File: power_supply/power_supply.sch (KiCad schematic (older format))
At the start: 39 parts, among them J1 Conn_01x04_Male, J2 Conn_01x03_Male, J3 Conn_01x03_Male, J4 Conn_01x03_Male, U1 LM7815_TO220, U2 LM7915_TO220, U3 LM7805_TO220

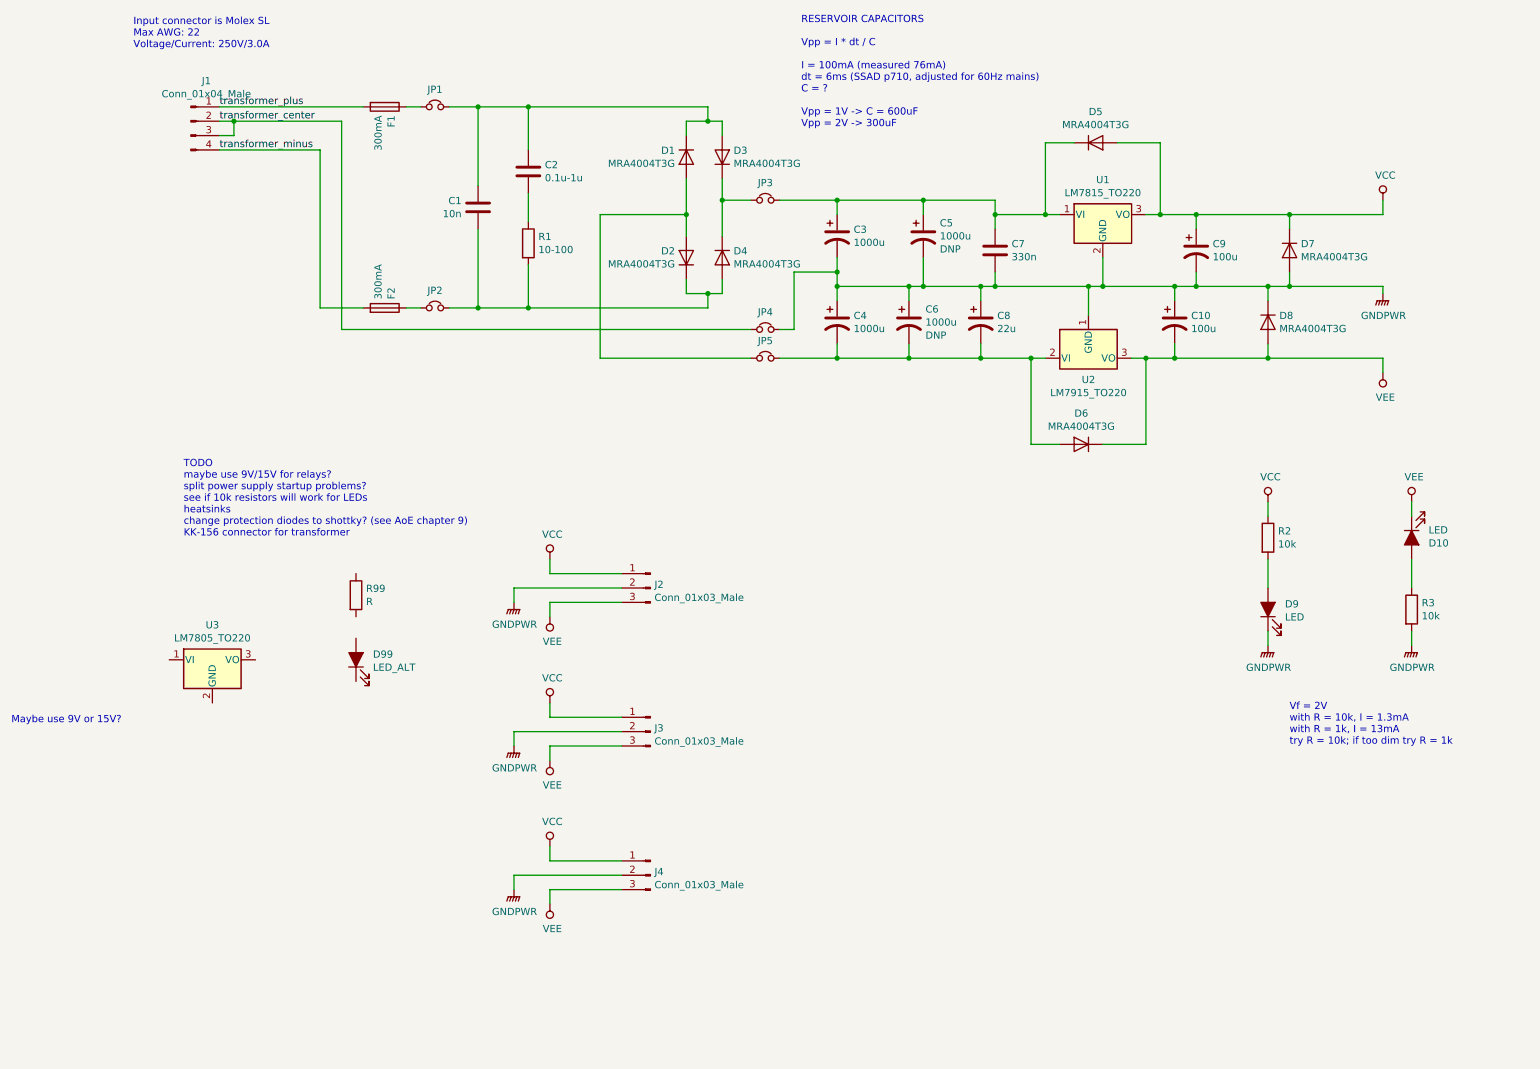
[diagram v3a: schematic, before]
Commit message: Update power supply layout & schematic
- Update snubber capacitor circuit details
- add heatsinks & mounting holes to schematic (footprints incorrect or
missing)
- initial component placement in layout
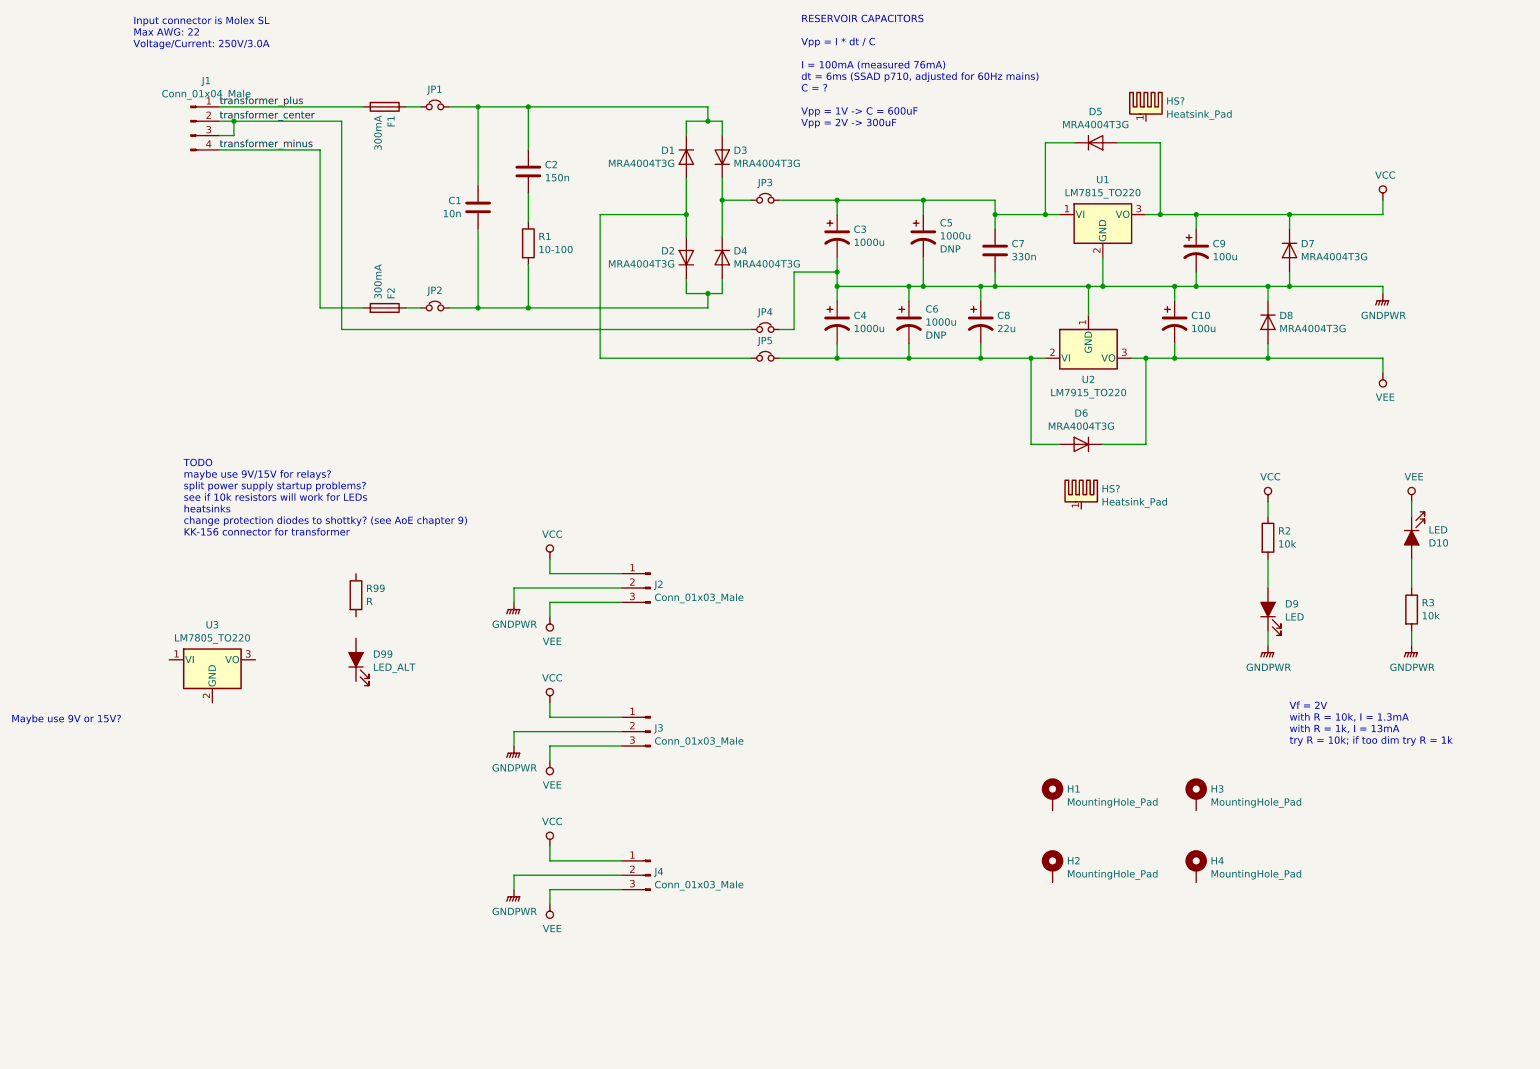
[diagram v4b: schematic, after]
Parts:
- added H1, H2, H3, H4: MountingHole_Pad, MountingHole:MountingHole_4.3mm_M4_Pad, symbol Mechanical:MountingHole_Pad
- added HS? (x2): Heatsink_Pad, symbol Mechanical:Heatsink_Pad
- C1: footprint (none) -> Capacitor_THT:C_Rect_L7.2mm_W2.5mm_P5.00mm_FKS2_FKP2_MKS2_MKP2; Distributor (none) -> Digikey; Distributor PN (none) -> 495-1180-ND; Manufacturer (none) -> EPCOS; Manufacturer PN (none) -> B32529C3103J000; URL (none) -> https://www.digikey.com/product-detail/en/B32529C3103J000/4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; Unit Price (none) -> 0.31
- C2: value 0.1u-1u -> 150n; footprint (none) -> Capacitor_THT:C_Rect_L7.5mm_W6.5mm_P5.00mm; Distributor (none) -> Digikey; Distributor PN (none) -> 495-2535-ND; Manufacturer (none) -> EPCOS; Manufacturer PN (none) -> B32529C3154K000; URL (none) -> https://www.digikey.com/product-detail/en/B32529C3154K000/4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; Unit Price (none) -> 0.63
- R1: footprint (none) -> Resistor_SMD:R_1206_3216Metric_Pad1.42x1.75mm_HandSolder
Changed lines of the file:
@@
 P 3350 1700
 F 0 "C2" H 3465 1746 50  0000 L CNN
-F 1 "0.1u-1u" H 3465 1655 50  0000 L CNN
-F 2 "" H 3388 1550 50  0001 C CNN
-F 3 "~" H 3350 1700 50  0001 C CNN
+F 1 "150n" H 3465 1655 50  0000 L CNN
+F 2 "Capacitor_THT:C_Rect_L7.5mm_W6.5mm_P5.00mm" H 3388 1550 50  0001 C CNN
+F 3 "https://www.tdk-electronics.tdk.com/inf/20/20/db/fc_2009/B32520_529.pdf" H 3350 1700 50  0001 C CNN
+F 4 "EPCOS" H 3350 1700 50  0001 C CNN "Manufacturer"
+F 5 "B32529C3154K000" H 3350 1700 50  0001 C CNN "Manufacturer PN"
+F 6 "Digikey" H 3350 1700 50  0001 C CNN "Distributor"
+F 7 "495-2535-ND" H 3350 1700 50  0001 C CNN "Distributor PN"
+F 8 "https://www.digikey.com/product-detail/en/B32529C3154K000/495-2535-ND/1089815/?itemSeq=288794403" H 3350 1700 50  0001 C CNN "URL"
+F 9 "0.63" H 3350 1700 50  0001 C CNN "Unit Price"
 	1    3350 1700
 	1    0    0    -1
@@
 F 0 "R1" H 3420 2246 50  0000 L CNN
 F 1 "10-100" H 3420 2155 50  0000 L CNN
-F 2 "" V 3280 2200 50  0001 C CNN
+F 2 "Resistor_SMD:R_1206_3216Metric_Pad1.42x1.75mm_HandSolder" V 3280 2200 50  0001 C CNN
 F 3 "~" H 3350 2200 50  0001 C CNN
 	1    3350 2200
@@
 F 0 "C1" H 3115 1996 50  0000 L CNN
 F 1 "10n" H 3115 1905 50  0000 L CNN
-F 2 "" H 3038 1800 50  0001 C CNN
-F 3 "~" H 3000 1950 50  0001 C CNN
+F 2 "Capacitor_THT:C_Rect_L7.2mm_W2.5mm_P5.00mm_FKS2_FKP2_MKS2_MKP2" H 3038 1800 50  0001 C CNN
+F 3 "https://www.tdk-electronics.tdk.com/inf/20/20/db/fc_2009/B32520_529.pdf" H 3000 1950 50  0001 C CNN
+F 4 "EPCOS" H 3000 1950 50  0001 C CNN "Manufacturer"
+F 5 "B32529C3103J000" H 3000 1950 50  0001 C CNN "Manufacturer PN"
+F 6 "Digikey" H 3000 1950 50  0001 C CNN "Distributor"
+F 7 "495-1180-ND" H 3000 1950 50  0001 C CNN "Distributor PN"
+F 8 "https://www.digikey.com/product-detail/en/B32529C3103J000/495-1180-ND/592757/?itemSeq=288794392" H 3000 1950 50  0001 C CNN "URL"
+F 9 "0.31" H 3000 1950 50  0001 C CNN "Unit Price"
 	1    3000 1950
 	-1   0    0    -1
@@
 	1    0    0    -1
 $EndComp
+$Comp
+L Mechanical:MountingHole_Pad H1
+U 1 1 5CB49A9B
+P 7000 6050
+F 0 "H1" H 7100 6099 50  0000 L CNN
+F 1 "MountingHole_Pad" H 7100 6008 50  0000 L CNN
+F 2 "MountingHole:MountingHole_4.3mm_M4_Pad" H 7000 6050 50  0001 C CNN
+F 3 "~" H 7000 6050 50  0001 C CNN
+	1    7000 6050
+	1    0    0    -1
+$EndComp
+$Comp
+L Mechanical:MountingHole_Pad H3
+U 1 1 5CB4A635
+P 8000 6050
+F 0 "H3" H 8100 6099 50  0000 L CNN
+F 1 "MountingHole_Pad" H 8100 6008 50  0000 L CNN
+F 2 "MountingHole:MountingHole_4.3mm_M4_Pad" H 8000 6050 50  0001 C CNN
+F 3 "~" H 8000 6050 50  0001 C CNN
+	1    8000 6050
+	1    0    0    -1
+$EndComp
+$Comp
+L Mechanical:MountingHole_Pad H4
+U 1 1 5CB4B51D
+P 8000 6550
+F 0 "H4" H 8100 6599 50  0000 L CNN
+F 1 "MountingHole_Pad" H 8100 6508 50  0000 L CNN
+F 2 "MountingHole:MountingHole_4.3mm_M4_Pad" H 8000 6550 50  0001 C CNN
+F 3 "~" H 8000 6550 50  0001 C CNN
+	1    8000 6550
+	1    0    0    -1
+$EndComp
+$Comp
+L Mechanical:MountingHole_Pad H2
+U 1 1 5CB4BFA5
+P 7000 6550
+F 0 "H2" H 7100 6599 50  0000 L CNN
+F 1 "MountingHole_Pad" H 7100 6508 50  0000 L CNN
+F 2 "MountingHole:MountingHole_4.3mm_M4_Pad" H 7000 6550 50  0001 C CNN
+F 3 "~" H 7000 6550 50  0001 C CNN
+	1    7000 6550
+	1    0    0    -1
+$EndComp
+$Comp
+L Mechanical:Heatsink_Pad HS?
+U 1 1 5CB4FC2E
+P 7200 3950
+F 0 "HS?" H 7341 3989 50  0000 L CNN
+F 1 "Heatsink_Pad" H 7341 3898 50  0000 L CNN
+F 2 "" H 7212 3900 50  0001 C CNN
+F 3 "~" H 7212 3900 50  0001 C CNN
+	1    7200 3950
+	1    0    0    -1
+$EndComp
+$Comp
+L Mechanical:Heatsink_Pad HS?
+U 1 1 5CB5054C
+P 7650 1250
+F 0 "HS?" H 7791 1289 50  0000 L CNN
+F 1 "Heatsink_Pad" H 7791 1198 50  0000 L CNN
+F 2 "" H 7662 1200 50  0001 C CNN
+F 3 "~" H 7662 1200 50  0001 C CNN
+	1    7650 1250
+	1    0    0    -1
+$EndComp
